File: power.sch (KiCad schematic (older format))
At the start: 65 parts, among them J1 PJ-202AH, J2 PJ-002B, J4 Screw_Terminal_01x10, U11 LT3471, U12 ADP2300AUJZ-R7, U13 LM317LIPKG3, U14 LP38693MP-5.0, U15 ADP150AUJZ-3.3-R7, U16 ADR395AUJZ-REEL7, U17 LM2937xMP, U18 LM337LMX_NOPB, U19 MAX6070BAUT21+T, U20 LP5907MFX-1.8, U21 MC79M15_TO252, U34 INA199C2DCKT

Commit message: completed gp adc
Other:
- note added: "Allows for observation \nor override of supplies\n"
- note removed: "Allows for observation \n\nor override of supplies\n"
- moved on the sheet: C49, C50, R133, R41, R42

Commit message: add 2.5 V supply
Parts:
- removed R133: 20m, Resistor_SMD:R_0603_1608Metric, symbol Device:R_US
- removed U34: INA199C2DCKT, adc_dac_v1:DCK6_TEX, symbol adc_dac_v1-eagle-import:INA199C2DCKT
- added C?: 0.33u, Capacitor_SMD:C_0603_1608Metric, symbol Device:C
- added C?: 0.1u, Capacitor_SMD:C_0603_1608Metric, symbol Device:C
- added R?: 100k, Resistor_SMD:R_0603_1608Metric, symbol Device:R_US
- added U?: LP38693MP-2.5, Package_TO_SOT_SMD:SOT-223-5, symbol Regulator_Linear:LP38693MP-2.5
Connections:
- net labels added: +2V5, EN_2V5
- net labels removed: 5V_ISENSE, 5V_SENSE
- wire segments 214 -> 215
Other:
- note removed: "100 V/V gain"
- moved on the sheet: J2, J4

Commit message: modify LVDS connections for AD7960
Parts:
- U19: symbol adc_dac_v1-eagle-import:MAX6070BAUT21+T -> covg-kicad:MAX6070BAUT21+T
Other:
- note added: "500 mA output\nneeded for FPGA LVDS bank"
- note added: "Used by fast ADC"
- moved on the sheet: C46, J4
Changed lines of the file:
@@
 L power:GND #GND069
 U 1 1 E32AEC55
-P 8900 4850
-F 0 "#GND069" H 8900 4850 50  0001 C CNN
-F 1 "GND" H 8800 4750 59  0001 L BNN
-F 2 "" H 8900 4850 50  0001 C CNN
-F 3 "" H 8900 4850 50  0001 C CNN
-	1    8900 4850
+P 8800 4700
+F 0 "#GND069" H 8800 4700 50  0001 C CNN
+F 1 "GND" H 8700 4600 59  0001 L BNN
+F 2 "" H 8800 4700 50  0001 C CNN
+F 3 "" H 8800 4700 50  0001 C CNN
+	1    8800 4700
 	1    0    0    -1
 $EndComp
@@
 L Device:C C46
 U 1 1 07389C7E
-P 9100 4350
-F 0 "C46" H 9140 4375 59  0000 L BNN
-F 1 "0.1u" H 9140 4185 59  0000 L BNN
-F 2 "Capacitor_SMD:C_0603_1608Metric" H 9100 4350 50  0001 C CNN
-F 3 "" H 9100 4350 50  0001 C CNN
-	1    9100 4350
+P 9500 4150
+F 0 "C46" H 9540 4175 59  0000 L BNN
+F 1 "0.1u" H 9540 3985 59  0000 L BNN
+F 2 "Capacitor_SMD:C_0603_1608Metric" H 9500 4150 50  0001 C CNN
+F 3 "" H 9500 4150 50  0001 C CNN
+	1    9500 4150
 	1    0    0    -1
 $EndComp
@@
 $EndComp
 $Comp
-L adc_dac_v1-eagle-import:MAX6070BAUT21+T U19
+L covg-kicad:MAX6070BAUT21+T U19
 U 1 1 32B63AAA
-P 6900 4050
-F 0 "U19" H 7614 4409 69  0000 L BNN
-F 1 "MAX6070BAUT21+T" H 7589 4309 69  0000 L BNN
-F 2 "adc_dac_v1:21-0058I_MXM" H 6900 4050 50  0001 C CNN
-F 3 "" H 6900 4050 50  0001 C CNN
-	1    6900 4050
+P 6800 3900
+F 0 "U19" H 7514 4259 69  0000 L BNN
+F 1 "MAX6070BAUT21+T" H 7489 4159 69  0000 L BNN
+F 2 "adc_dac_v1:21-0058I_MXM" H 6800 3900 50  0001 C CNN
+F 3 "" H 6800 3900 50  0001 C CNN
+	1    6800 3900
 	1    0    0    -1
 $EndComp
@@
 Text GLabel 4000 4850 2    70   BiDi ~ 0
 5V_REF
-Text GLabel 9100 4050 2    70   BiDi ~ 0
+Text GLabel 9000 3900 2    47   BiDi ~ 0
 2V048_REF
 Text GLabel 3150 7700 2    70   BiDi ~ 0
@@
 	4200 5250 4400 5250
 Wire Wire Line
-	8900 4550 8600 4550
-Wire Wire Line
-	8900 4550 9100 4550
+	8800 4200 8500 4200
+Wire Wire Line
+	8800 4200 8800 4300
 Wire Wire Line
 	1200 1050 1100 1050
@@
 	4800 6900 4700 6900
 Wire Wire Line
-	11650 2450 11950 2450
-Wire Wire Line
-	11650 2350 11950 2350
-Wire Wire Line
-	11450 1750 11950 1750
-Wire Wire Line
-	7000 4150 6800 4150
+	11200 3550 11500 3550
+Wire Wire Line
+	11200 3450 11500 3450
+Wire Wire Line
+	11000 2850 11500 2850
+Wire Wire Line
+	6800 4000 6800 4150
 Wire Wire Line
 	6800 4150 6500 4150
 Wire Wire Line
-	7000 4350 6800 4350
-Wire Wire Line
-	6800 4350 6800 4150
-Wire Wire Line
-	11950 2050 11750 2050
+	6800 4200 6800 4150
+Wire Wire Line
+	11500 3150 11300 3150
 Wire Wire Line
 	6850 900  6950 900
 Wire Wire Line
-	11950 1950 11550 1950
-Wire Wire Line
-	11950 1850 11900 1850
+	11500 3050 11100 3050
+Wire Wire Line
+	11500 2950 11450 2950
 Wire Wire Line
 	1900 950  1900 850
@@
 	2550 7050 2850 7050
 Wire Wire Line
-	11950 2250 11550 2250
+	11500 3350 11100 3350
 Wire Wire Line
 	3900 4850 4000 4850
@@
 	4000 4950 4000 4850
 Wire Wire Line
-	8600 4050 9100 4050
-Wire Wire Line
-	8600 4150 9100 4150
-Wire Wire Line
-	9100 4150 9100 4050
+	8500 3900 9000 3900
+Wire Wire Line
+	8500 4000 9000 4000
+Wire Wire Line
+	9000 4000 9000 3900
 Wire Wire Line
 	2550 8000 2650 8000
@@
 Connection ~ 10500 6000
 Connection ~ 9500 6600
-Connection ~ 8900 4550
 Connection ~ 6800 4150
 Connection ~ 1050 7700
@@
 	11600 6400 11600 6600
 Wire Wire Line
-	9100 4200 9100 4150
-Connection ~ 9100 4150
-Wire Wire Line
-	9100 4500 9100 4550
-Wire Wire Line
-	8900 4550 8900 4850
+	9500 4000 9000 4000
+Connection ~ 9000 4000
+Wire Wire Line
+	9500 4300 8800 4300
 Wire Wire Line
 	650  8100 650  8300
@@
 L power:+15V #PWR0128
 U 1 1 61215EF4
-P 11550 2250
-F 0 "#PWR0128" H 11550 2100 50  0001 C CNN
-F 1 "+15V" V 11565 2378 50  0000 L CNN
-F 2 "" H 11550 2250 50  0001 C CNN
-F 3 "" H 11550 2250 50  0001 C CNN
-	1    11550 2250
+P 11100 3350
+F 0 "#PWR0128" H 11100 3200 50  0001 C CNN
+F 1 "+15V" V 11115 3478 50  0000 L CNN
+F 2 "" H 11100 3350 50  0001 C CNN
+F 3 "" H 11100 3350 50  0001 C CNN
+	1    11100 3350
 	0    -1   -1   0
 $EndComp
@@
 L power:-15V #PWR0129
 U 1 1 61216E43
-P 11550 2150
-F 0 "#PWR0129" H 11550 2250 50  0001 C CNN
-F 1 "-15V" V 11565 2278 50  0000 L CNN
-F 2 "" H 11550 2150 50  0001 C CNN
-F 3 "" H 11550 2150 50  0001 C CNN
-	1    11550 2150
+P 11100 3250
+F 0 "#PWR0129" H 11100 3350 50  0001 C CNN
+F 1 "-15V" V 11115 3378 50  0000 L CNN
+F 2 "" H 11100 3250 50  0001 C CNN
+F 3 "" H 11100 3250 50  0001 C CNN
+	1    11100 3250
 	0    -1   -1   0
 $EndComp
@@
 L power:+3V3 #PWR0130
 U 1 1 61217D14
-P 11550 1950
-F 0 "#PWR0130" H 11550 1800 50  0001 C CNN
-F 1 "+3V3" V 11565 2078 50  0000 L CNN
-F 2 "" H 11550 1950 50  0001 C CNN
-F 3 "" H 11550 1950 50  0001 C CNN
-	1    11550 1950
+P 11100 3050
+F 0 "#PWR0130" H 11100 2900 50  0001 C CNN
+F 1 "+3V3" V 11115 3178 50  0000 L CNN
+F 2 "" H 11100 3050 50  0001 C CNN
+F 3 "" H 11100 3050 50  0001 C CNN
+	1    11100 3050
 	0    -1   -1   0
 $EndComp
@@
 L power:+5V #PWR0131
 U 1 1 612190C3
-P 11750 2050
-F 0 "#PWR0131" H 11750 1900 50  0001 C CNN
-F 1 "+5V" V 11765 2178 50  0000 L CNN
-F 2 "" H 11750 2050 50  0001 C CNN
-F 3 "" H 11750 2050 50  0001 C CNN
-	1    11750 2050
+P 11300 3150
+F 0 "#PWR0131" H 11300 3000 50  0001 C CNN
+F 1 "+5V" V 11315 3278 50  0000 L CNN
+F 2 "" H 11300 3150 50  0001 C CNN
+F 3 "" H 11300 3150 50  0001 C CNN
+	1    11300 3150
 	0    -1   -1   0
 $EndComp
@@
 Connection ~ 6500 4150
 Wire Wire Line
-	6100 3900 7000 3900
-Wire Wire Line
-	7000 3900 7000 4050
-Wire Wire Line
 	6100 3900 6100 4100
 $Comp
@@
 L power:+1V8 #PWR0142
 U 1 1 61303020
-P 11900 1850
-F 0 "#PWR0142" H 11900 1700 50  0001 C CNN
-F 1 "+1V8" V 11915 1978 50  0000 L CNN
-F 2 "" H 11900 1850 50  0001 C CNN
-F 3 "" H 11900 1850 50  0001 C CNN
-	1    11900 1850
+P 11450 2950
+F 0 "#PWR0142" H 11450 2800 50  0001 C CNN
+F 1 "+1V8" V 11465 3078 50  0000 L CNN
+F 2 "" H 11450 2950 50  0001 C CNN
+F 3 "" H 11450 2950 50  0001 C CNN
+	1    11450 2950
 	0    -1   -1   0
 $EndComp
@@
 NoConn ~ 4700 6800
 Wire Wire Line
-	11550 2150 11950 2150
+	11100 3250 11500 3250
 $Comp
 L Device:R_US R30
@@
 Wire Wire Line
 	9000 2300 9000 2450
-Text Notes 9850 2900 0    50   ~ 0
+Text Notes 9650 2800 0    50   ~ 0
 0.5 A output max\n\n1.1 V dropout
 $Comp
@@
 Wire Wire Line
 	6050 3250 6050 3200
-Text Label 11650 2350 0    50   ~ 0
+Text Label 11200 3450 0    50   ~ 0
 -16V5
-Text Label 11700 2450 0    50   ~ 0
+Text Label 11250 3550 0    50   ~ 0
 16V5
 Wire Wire Line
-	11650 2550 11950 2550
-Text Label 11700 2550 0    50   ~ 0
+	11200 3650 11500 3650
+Text Label 11250 3650 0    50   ~ 0
 6V_IN
 $Comp
 L Connector:Screw_Terminal_01x10 J4
 U 1 1 619BFFB5
-P 12150 2150
-F 0 "J4" H 12230 2142 50  0000 L CNN
-F 1 "Screw_Terminal_01x10" H 12230 2051 50  0000 L CNN
-F 2 "" H 12150 2150 50  0001 C CNN
-F 3 "~" H 12150 2150 50  0001 C CNN
-	1    12150 2150
+P 11700 3250
+F 0 "J4" H 11780 3242 50  0000 L CNN
+F 1 "Screw_Terminal_01x10" H 11780 3151 50  0000 L CNN
+F 2 "" H 11700 3250 50  0001 C CNN
+F 3 "~" H 11700 3250 50  0001 C CNN
+	1    11700 3250
 	1    0    0    -1
 $EndComp
@@
 L power:GND #GND0114
 U 1 1 619C2994
-P 11450 2650
-F 0 "#GND0114" H 11450 2650 50  0001 C CNN
-F 1 "GND" H 11350 2550 59  0001 L BNN
-F 2 "" H 11450 2650 50  0001 C CNN
-F 3 "" H 11450 2650 50  0001 C CNN
-	1    11450 2650
+P 11000 3750
+F 0 "#GND0114" H 11000 3750 50  0001 C CNN
+F 1 "GND" H 10900 3650 59  0001 L BNN
+F 2 "" H 11000 3750 50  0001 C CNN
+F 3 "" H 11000 3750 50  0001 C CNN
+	1    11000 3750
 	0    1    1    0
 $EndComp
 Wire Wire Line
-	11450 2650 11950 2650
-Text Notes 11450 3100 0    50   ~ 0
+	11000 3750 11500 3750
+Text Notes 11250 4000 0    50   ~ 0
 Allows for observation \nor override of supplies\n
 $Comp
@@
 	1    0    0    -1
 $EndComp
-Text Notes 11750 850  0    59   ~ 0
-500 mA output
+Text Notes 11750 850  0    39   ~ 0
+500 mA output\nneeded for FPGA LVDS bank
 Wire Wire Line
 	11700 1300 11700 1400
@@
 L power:+2V5 #PWR?
 U 1 1 60C2A239
-P 11450 1750
-F 0 "#PWR?" H 11450 1600 50  0001 C CNN
-F 1 "+2V5" V 11465 1878 50  0000 L CNN
-F 2 "" H 11450 1750 50  0001 C CNN
-F 3 "" H 11450 1750 50  0001 C CNN
-	1    11450 1750
+P 11000 2850
+F 0 "#PWR?" H 11000 2700 50  0001 C CNN
+F 1 "+2V5" V 11015 2978 50  0000 L CNN
+F 2 "" H 11000 2850 50  0001 C CNN
+F 3 "" H 11000 2850 50  0001 C CNN
+	1    11000 2850
 	0    -1   -1   0
 $EndComp
+Text Notes 2250 5450 0    118  ~ 0
+Used by fast ADC
+Wire Wire Line
+	6100 3900 7150 3900
+Wire Wire Line
+	6800 4000 7150 4000
+Wire Wire Line
+	6800 4200 7150 4200
+Connection ~ 8800 4300
+Wire Wire Line
+	8800 4300 8800 4700
 $EndSCHEMATC

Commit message: moved level shifters to FPGA
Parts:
- removed C28, C30: 4.7u, Capacitor_SMD:C_0603_1608Metric, symbol Device:C
- removed C29, C38, C39, C49, C50: 0.1u, Capacitor_SMD:C_0603_1608Metric, symbol Device:C
- removed C31: 10u, Capacitor_SMD:C_0603_1608Metric, symbol Device:C
- removed D1: PD3S130, adc_dac_v1:POWERDI323, symbol adc_dac_v1-eagle-import:PD3S160
- removed J1: PJ-202AH, adc_dac_v1:CUI_PJ-202AH, symbol adc_dac_v1-eagle-import:PJ-202AH
- removed L1: SRR4028-4R7Y, adc_dac_v1:IND_BOURNS_SRR4028, symbol adc_dac_v1-eagle-import:SRR4028-4R7Y
- removed R25: 21.5k, Resistor_SMD:R_0603_1608Metric, symbol Device:R_US
- removed R26: 10.2k, Resistor_SMD:R_0603_1608Metric, symbol Device:R_US
- removed R27: 2.26k, Resistor_SMD:R_0603_1608Metric, symbol Device:R_US
- removed R28: 10.5k, Resistor_SMD:R_0603_1608Metric, symbol Device:R_US
- removed R41: 240, Resistor_SMD:R_0603_1608Metric, symbol Device:R_US
- removed R42: 1k, Resistor_SMD:R_0603_1608Metric, symbol Device:R_US
- removed U12: ADP2300AUJZ-R7, adc_dac_v1:UJ_6_ADI, symbol adc_dac_v1-eagle-import:ADP2300AUJZ-R7
- removed U13: LM317LIPKG3, adc_dac_v1:PK3_TEX, symbol adc_dac_v1-eagle-import:LM317LIPKG3
- removed U18: LM337LMX_NOPB, adc_dac_v1:M08A_TEX, symbol adc_dac_v1-eagle-import:LM337LMX_NOPB
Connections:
- net labels removed: -6V5, 18V_IN, 7V5_IN, AMP_PWR+, AMP_PWR-
- wire segments 215 -> 151
- no-connect marks 4 -> 1
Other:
- note added: "+/-10 mA output current"
- note removed: "3-20V input"
- note removed: "7.5 V External Supply\n18 V External Supply"
- note removed: "For FET gate drive \n(low leakage gate drive)"
- moved on the sheet: C10, C11, C12, C32, C33, C34, C35, C36, C37, C40, C41, C42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

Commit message: updates to high-speed DAC
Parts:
- removed C44: 0.1u, Capacitor_SMD:C_0603_1608Metric, symbol Device:C
- removed U16: ADR395AUJZ-REEL7, adc_dac_v1:UJ_5_ADI, symbol adc_dac_v1-eagle-import:ADR395AUJZ-REEL7
- added R? (x2): 100k, Resistor_SMD:R_0603_1608Metric, symbol Device:R_US
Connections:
- net labels added: EN_1V8, EN_3V3
- net labels removed: 5V_REF
- wire segments 151 -> 141
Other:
- note removed: "Used by fast ADC"
- moved on the sheet: C34, C36, C41, C46, C47, C48, C?, R23, R?

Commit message: gain adjust for general purpose dac
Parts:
- added C? (x2): 0.33u, Capacitor_SMD:C_0603_1608Metric, symbol Device:C
- added FB?: Ferrite_Bead, Capacitor_SMD:C_1206_3216Metric, symbol Device:Ferrite_Bead
- added R? (x2): 4.7k, Resistor_SMD:R_0603_1608Metric, symbol Device:R_US
- J4: value Screw_Terminal_01x10 -> Screw_Terminal_01x12; symbol Connector:Screw_Terminal_01x10 -> Connector:Screw_Terminal_01x12
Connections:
- net +15V: now also J4.8 (Pin_8); no longer J4.6 (Pin_6)
- net +2V5: now also J4.4 (Pin_4); no longer J4.1 (Pin_1)
- net +3V3: now also J4.5 (Pin_5); no longer J4.3 (Pin_3)
- net +5V: now also J4.6 (Pin_6); no longer J4.4 (Pin_4)
- net -15V: now also J4.7 (Pin_7); no longer J4.5 (Pin_5)
- net -16V5: now also J4.9 (Pin_9); no longer J4.7 (Pin_7)
- net 16V5: now also J4.10 (Pin_10); no longer J4.8 (Pin_8)
- net 2V048_REF: now also J4.3 (Pin_3)
- net 6V_IN: now also J4.11 (Pin_11), FB?.1; no longer J2.1, J4.9 (Pin_9)
- net GND: now also J4.1 (Pin_1), J4.12 (Pin_12), C?.2, C?.2; no longer J4.10 (Pin_10)
- net SHb_n: no longer names the net of R24.1, U11.7 (~SHDN~/SS2)
- net SHb_n: now also C?.1, R?.2
- net SHb_p: no longer names the net of R22.1, U11.9 (~SHDN~/SS1)
- net SHb_p: now also C?.1, R?.2
- new net: FB?.2, J2.1
- new net EN_15V: R?.1
- new net EN_n15V: R?.1
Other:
- moved on the sheet: R22

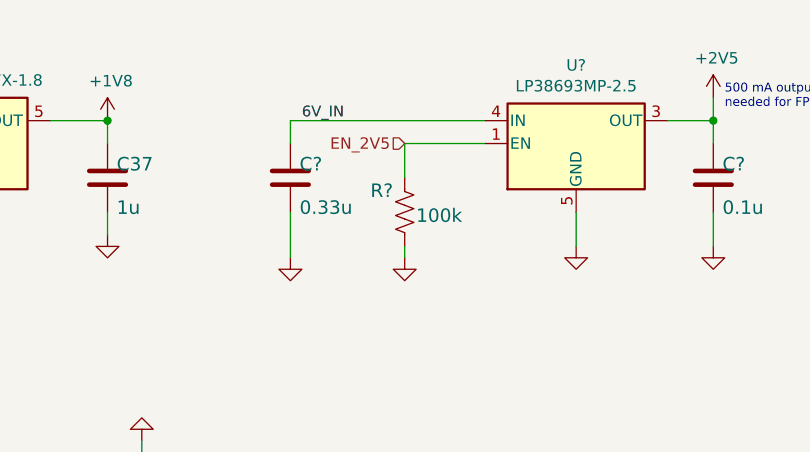
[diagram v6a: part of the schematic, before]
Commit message: updates to FPGA page
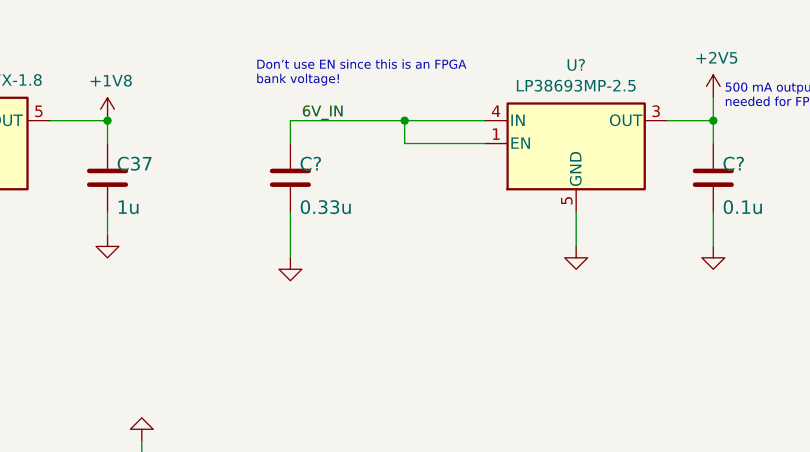
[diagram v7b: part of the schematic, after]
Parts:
- removed R?: 100k, Resistor_SMD:R_0603_1608Metric, symbol Device:R_US
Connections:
- net EN_2V5 is gone; now on net 6V_IN: U?.1 (EN)
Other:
- note added: "Don’t use EN since this is an FPGA\nbank voltage!"
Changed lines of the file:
@@
 	9650 2700 9650 2900
 Wire Wire Line
-	9650 2300 10500 2300
+	9650 2300 10150 2300
 Wire Wire Line
 	10500 2400 10150 2400
-$Comp
-L Device:R_US R?
-U 1 1 60BC23BA
-P 10150 2700
-F 0 "R?" H 10000 2759 59  0000 L BNN
-F 1 "100k" H 10200 2650 59  0000 L BNN
-F 2 "Resistor_SMD:R_0603_1608Metric" H 10150 2700 50  0001 C CNN
-F 3 "" H 10150 2700 50  0001 C CNN
-	1    10150 2700
-	1    0    0    -1
-$EndComp
-$Comp
-L power:GND #GND?
-U 1 1 60BC23C0
-P 10150 2900
-F 0 "#GND?" H 10150 2900 50  0001 C CNN
-F 1 "GND" H 10050 2800 59  0001 L BNN
-F 2 "" H 10150 2900 50  0001 C CNN
-F 3 "" H 10150 2900 50  0001 C CNN
-	1    10150 2900
-	1    0    0    -1
-$EndComp
-Wire Wire Line
-	10150 2900 10150 2850
 $Comp
 L Regulator_Linear:LP38693MP-2.5 U?
@@
 Text HLabel 7750 2400 0    50   Input ~ 0
 EN_1V8
-Wire Wire Line
-	10150 2400 10150 2550
-Text HLabel 10150 2400 0    50   Input ~ 0
-EN_2V5
 Wire Wire Line
 	10900 2700 10900 2850
@@
 Wire Wire Line
 	1150 2250 1100 2250
+Wire Wire Line
+	10150 2400 10150 2300
+Connection ~ 10150 2300
+Wire Wire Line
+	10150 2300 10500 2300
+Text Notes 9500 2150 0    39   ~ 0
+Don’t use EN since this is an FPGA\nbank voltage!
 $EndSCHEMATC
